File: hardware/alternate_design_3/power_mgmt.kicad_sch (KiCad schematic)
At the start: 2 parts, among them J2 Screw_Terminal_01x02, J3 Screw_Terminal_01x02

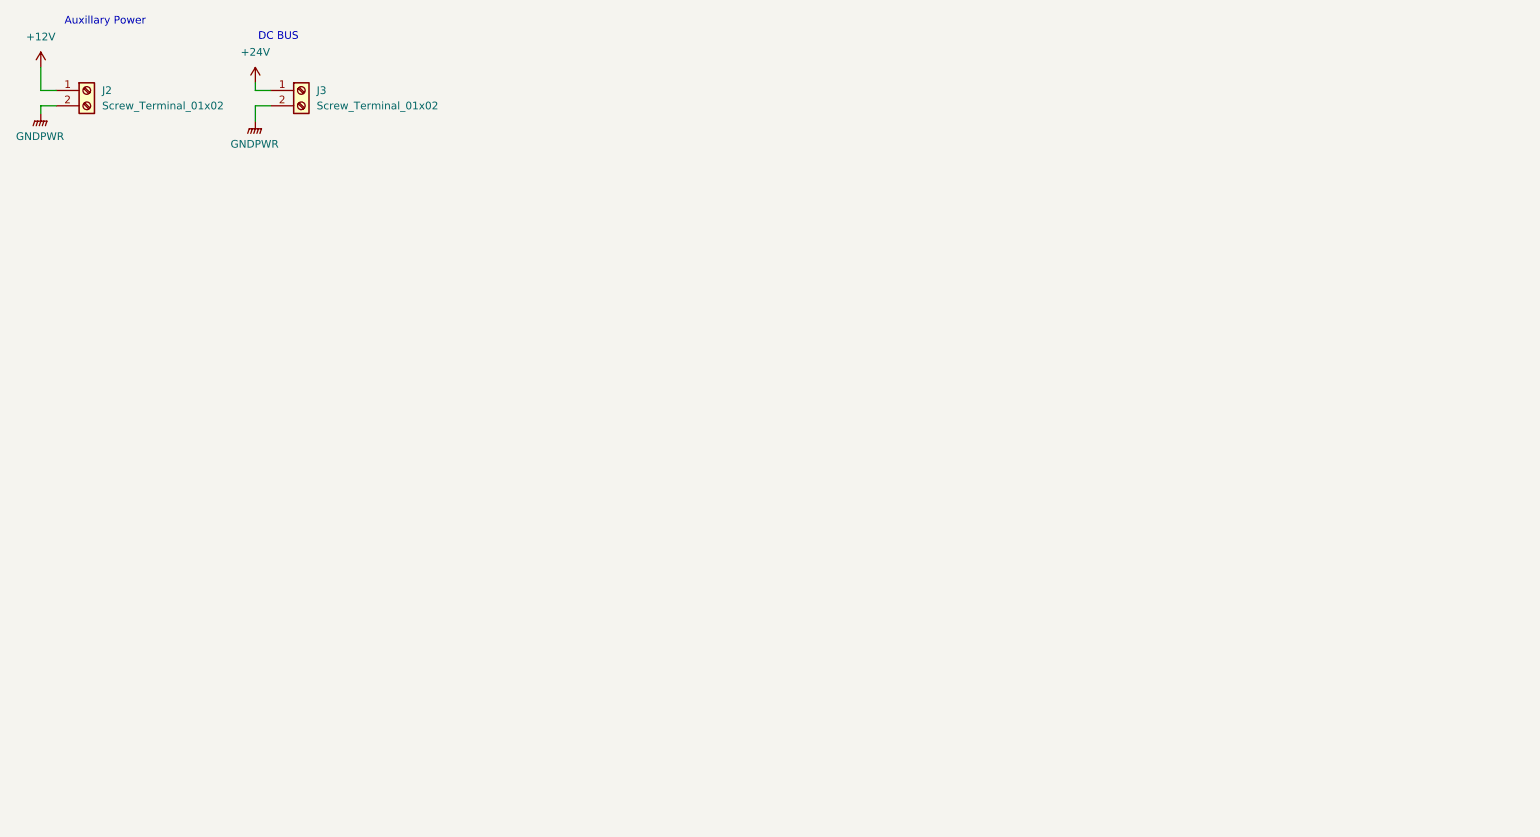
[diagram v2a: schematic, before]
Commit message: major additions to schematic of inverter
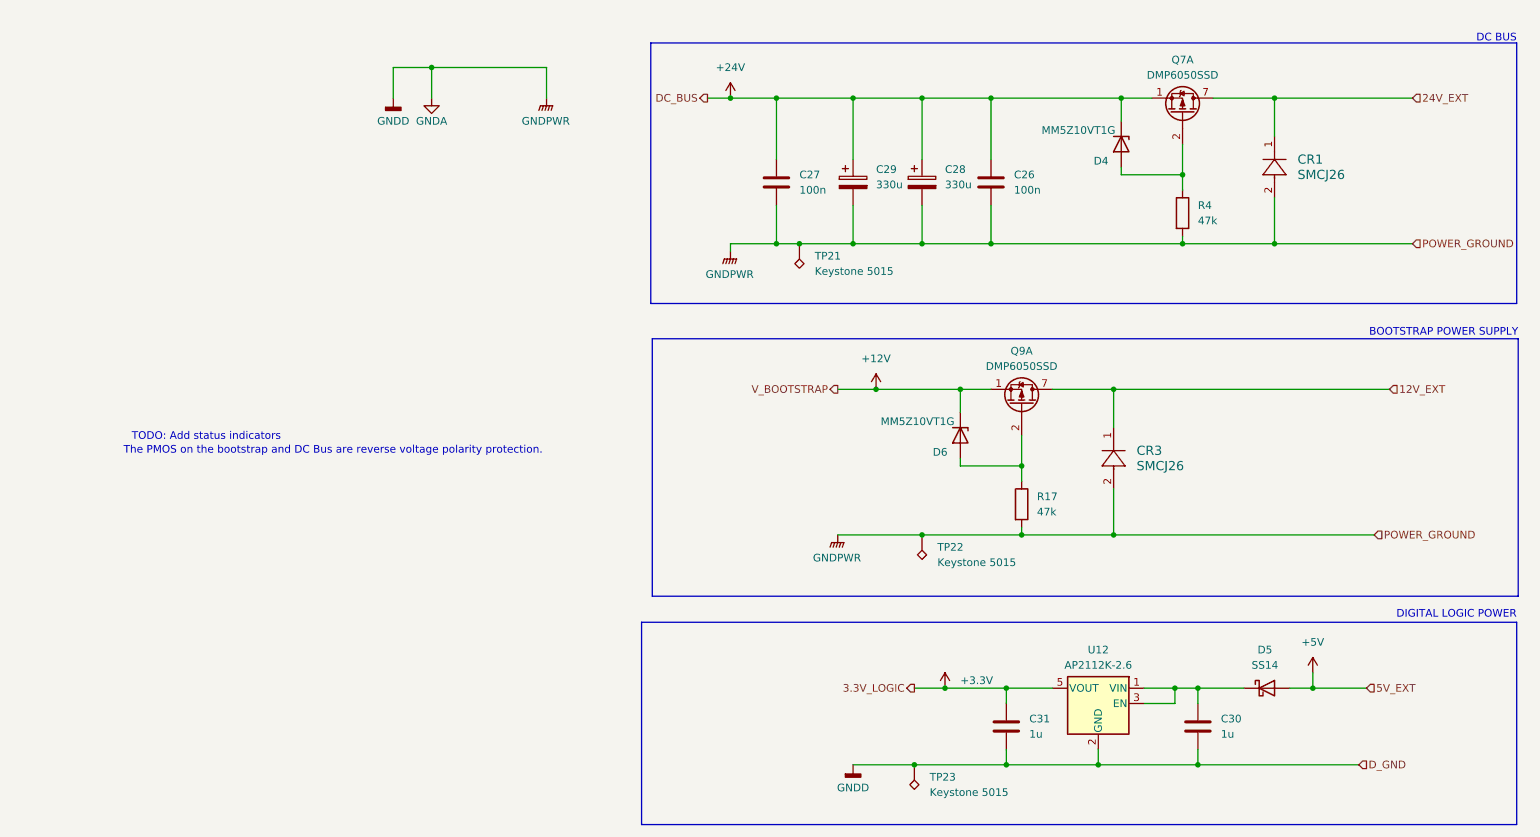
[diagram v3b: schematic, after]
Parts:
- removed J2, J3: Screw_Terminal_01x02, symbol Connector:Screw_Terminal_01x02
- added C26, C27: 100n, symbol Device:C
- added C28, C29: 330u, symbol Device:C_Polarized
- added C30, C31: 1u, symbol Device:C
- added CR1, CR3: SMCJ26, SMCJSeries_LTF, symbol symbols:SMCJ26
- added D4, D6: MM5Z10VT1G, Diode_SMD:D_SOD-523, symbol Diode:MM5Zxx
- added D5: SS14, Diode_SMD:D_SMA, symbol Diode:SS14
- added Q7, Q9: DMP6050SSD, Package_SO:SOIC-8_3.9x4.9mm_P1.27mm, symbol Transistor_FET:DMP6050SSD
- added R17, R4: 47k, symbol Device:R
- added TP21, TP22, TP23: Keystone 5015, symbol Connector:TestPoint_Alt
- added U12: AP2112K-2.6, Package_TO_SOT_SMD:SOT-23-5, symbol Regulator_Linear:AP2112K-2.6
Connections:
- net +12V: now also D6.1 (K), Q9.1 (S1)
- net +24V: now also C26.1, C27.1, C28.1, C29.1, D4.1 (K), Q7.1 (S1)
- new net: C30.1, D5.1 (K), U12.1 (VIN), U12.3 (EN)
- new net: D4.2 (A), Q7.2 (G1), R4.1
- new net: D6.2 (A), Q9.2 (G1), R17.1
- new net +3.3V: C31.1, U12.5 (VOUT)
- new net +5V: D5.2 (A)
- new net 12V_EXT: CR3.1, Q9.7 (D1), Q9.8 (D1)
- new net 24V_EXT: CR1.1, Q7.7 (D1), Q7.8 (D1)
- new net GNDA: C26.2, C27.2, C28.2, C29.2, C30.2, C31.2, CR1.2, CR3.2, R17.2, R4.2, TP21.1, TP22.1, TP23.1, U12.2 (GND)
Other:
- note added: "BOOTSTRAP POWER SUPPLY"
- note added: "DIGITAL LOGIC POWER"
- note added: "TODO: Add status indicators"
- note added: "The PMOS on the bootstrap and DC Bus are reverse voltage polarity protection."
- note removed: "Auxillary Power"
